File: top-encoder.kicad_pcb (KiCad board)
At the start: 2 copper layers, 8 x 8 mm, 8 parts, among them M1 THRU_HOLE_PAD, M2 THRU_HOLE_PAD, M3 THRU_HOLE_PAD, M4 THRU_HOLE_PAD, U2 TLE5009E1000FUMA1

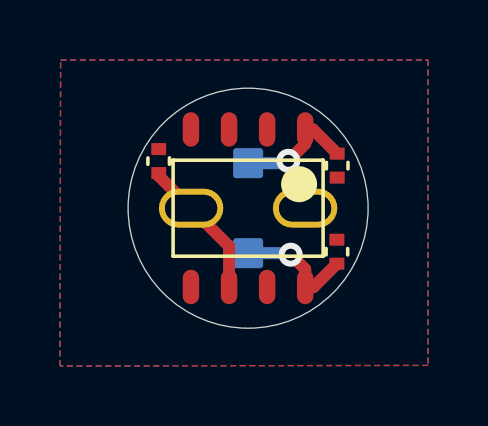
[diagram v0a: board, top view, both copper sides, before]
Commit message: updated pad spacing for 1mm for dogbone and baseplate
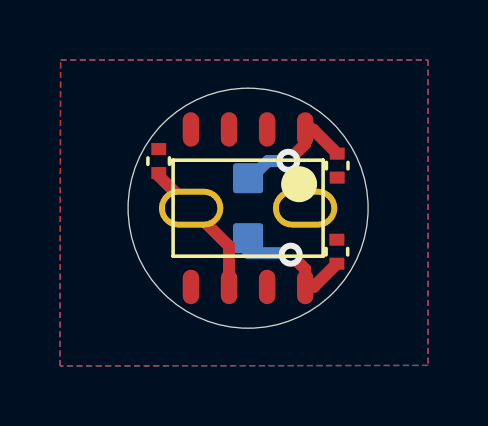
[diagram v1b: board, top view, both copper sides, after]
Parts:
- moved M2 0.50 mm to (142.0, 94.2)
- moved M3 0.50 mm to (142.0, 96.2)
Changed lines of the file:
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@@
   )
   (footprint "adapter-encoder:dogbone_pad" locked (layer "B.Cu")
-    (at 142.035 96.75 -90)
+    (at 142.035 96.25 -90)
     (property "Sheetfile" "top-encoder.kicad_sch")
     (property "Sheetname" "")
@@
   )
   (footprint "adapter-encoder:dogbone_pad" locked (layer "B.Cu")
-    (at 142.035 93.75 -90)
+    (at 142.035 94.25 -90)
     (property "Sheetfile" "top-encoder.kicad_sch")
     (property "Sheetname" "")
@@
   (segment (start 143.94 92.625) (end 144.2 92.625) (width 0.4) (layer "F.Cu") (net 2))
   (via (at 143.375 93.67) (size 0.8) (drill 0.4) (layers "F.Cu" "B.Cu") (net 2))
-  (segment (start 142.035 93.75) (end 143.295 93.75) (width 0.4) (layer "B.Cu") (net 2))
-  (segment (start 143.295 93.75) (end 143.375 93.67) (width 0.4) (layer "B.Cu") (net 2))
+  (segment (start 142.125 94.25) (end 142.695 93.68) (width 0.4) (layer "B.Cu") (net 2))
+  (segment (start 142.035 94.25) (end 142.125 94.25) (width 0.4) (layer "B.Cu") (net 2))
+  (segment (start 143.365 93.68) (end 143.375 93.67) (width 0.4) (layer "B.Cu") (net 2))
+  (segment (start 142.695 93.68) (end 143.365 93.68) (width 0.4) (layer "B.Cu") (net 2))
   (segment (start 144.22 97.875) (end 143.94 97.875) (width 0.4) (layer "F.Cu") (net 3))
   (segment (start 143.94 97.285) (end 143.455 96.8) (width 0.4) (layer "F.Cu") (net 3))
